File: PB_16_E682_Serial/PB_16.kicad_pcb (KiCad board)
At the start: 2 copper layers, 58 x 33 mm, 16 parts, among them J1 DMX1 RJ45, J2 DMX2 RJ45, J3 Serial In, SW1 DMX_Renard_Select, SW2 DMX_LOR_Select, U1 UA9638CP

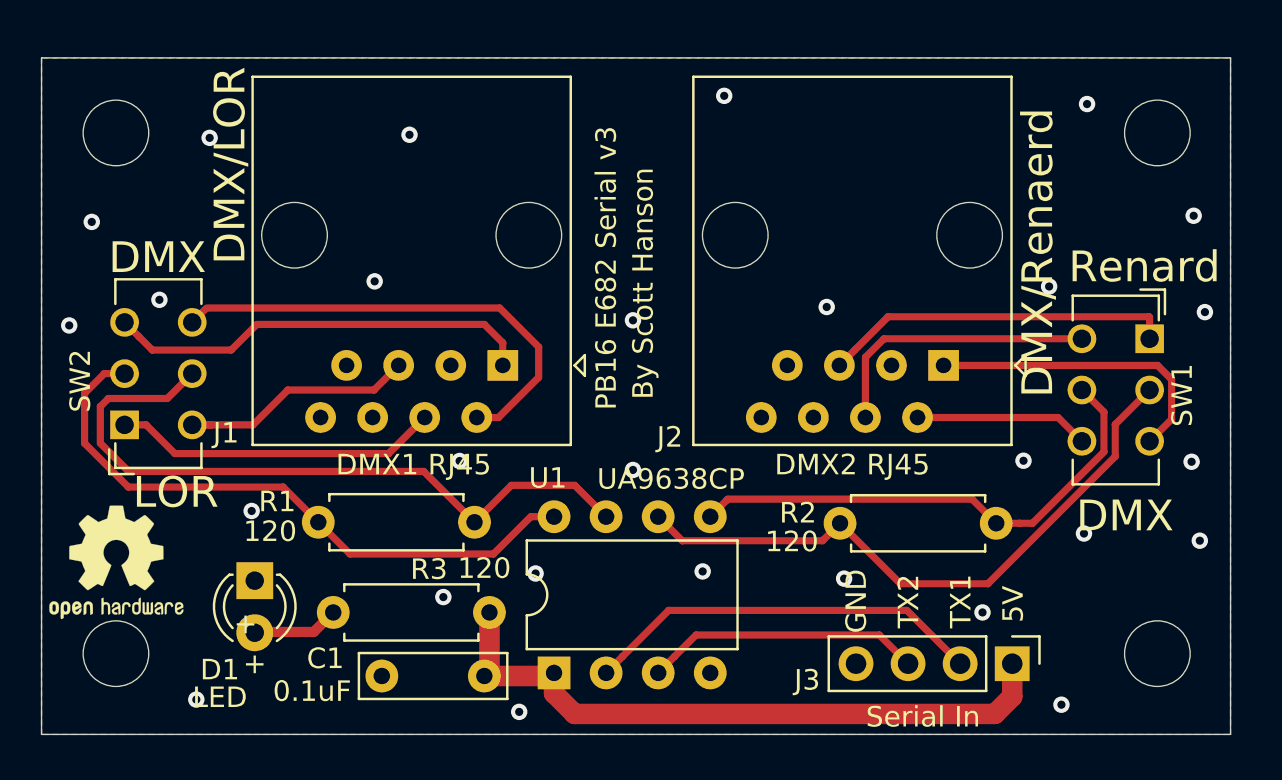
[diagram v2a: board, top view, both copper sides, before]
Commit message: increased mounting hole size
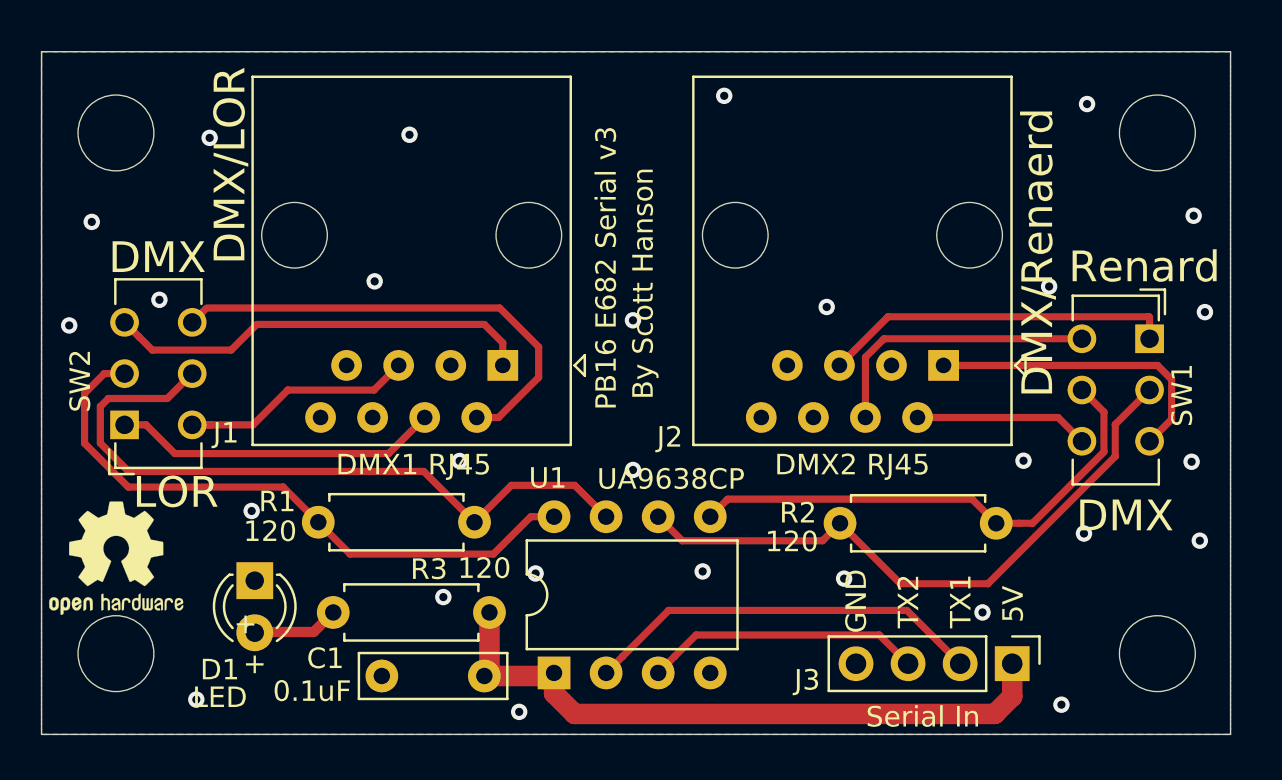
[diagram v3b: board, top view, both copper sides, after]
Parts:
- REF** (x4): value MountingHole_3.2mm_M3 -> MountingHole_3.7mm; footprint MountingHole:MountingHole_3.2mm_M3 -> MountingHole:MountingHole_3.7mm
- moved REF** 0.20 mm to (87.6, 94.4)
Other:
- board size 58 x 33 mm -> 58 x 33.3 mm
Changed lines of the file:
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@@
     (uvia_drill 0.1)
+  )
+  (module MountingHole:MountingHole_3.7mm (layer F.Cu)
+    (at 138.43 99.06)
+    (descr "Mounting Hole 3.7mm, no annular")
+    (tags "mounting hole 3.7mm no annular")
+    (attr virtual)
+    (fp_text reference REF** (at 0.57 5.94) (layer F.Fab)
+      (effects (font (size 1 1) (thickness 0.15)))
+    )
+    (fp_text value MountingHole_3.7mm (at 5.57 -4.06 90) (layer F.Fab)
+      (effects (font (size 1 1) (thickness 0.15)))
+    )
+    (fp_circle (center 0 0) (end 3.95 0) (layer F.CrtYd) (width 0.05))
+    (fp_circle (center 0 0) (end 3.7 0) (layer Cmts.User) (width 0.15))
+    (fp_text user %R (at 0.3 0) (layer F.Fab)
+      (effects (font (size 1 1) (thickness 0.15)))
+    )
+    (pad 1 np_thru_hole circle (at 0 0) (size 3.7 3.7) (drill 3.7) (layers *.Cu *.Mask))
+  )
+  (module MountingHole:MountingHole_3.7mm (layer F.Cu)
+    (at 138.43 73.66)
+    (descr "Mounting Hole 3.7mm, no annular")
+    (tags "mounting hole 3.7mm no annular")
+    (attr virtual)
+    (fp_text reference REF** (at 0 -4.2) (layer F.Fab)
+      (effects (font (size 1 1) (thickness 0.15)))
+    )
+    (fp_text value MountingHole_3.7mm (at -2.43 -6.66) (layer F.Fab)
+      (effects (font (size 1 1) (thickness 0.15)))
+    )
+    (fp_circle (center 0 0) (end 3.95 0) (layer F.CrtYd) (width 0.05))
+    (fp_circle (center 0 0) (end 3.7 0) (layer Cmts.User) (width 0.15))
+    (fp_text user %R (at 0.3 0) (layer F.Fab)
+      (effects (font (size 1 1) (thickness 0.15)))
+    )
+    (pad 1 np_thru_hole circle (at 0 0) (size 3.7 3.7) (drill 3.7) (layers *.Cu *.Mask))
+  )
+  (module MountingHole:MountingHole_3.7mm (layer F.Cu)
+    (at 87.63 73.66)
+    (descr "Mounting Hole 3.7mm, no annular")
+    (tags "mounting hole 3.7mm no annular")
+    (attr virtual)
+    (fp_text reference REF** (at -1.63 -5.66) (layer F.Fab)
+      (effects (font (size 1 1) (thickness 0.15)))
+    )
+    (fp_text value MountingHole_3.7mm (at -0.63 -4.66) (layer F.Fab)
+      (effects (font (size 1 1) (thickness 0.15)))
+    )
+    (fp_circle (center 0 0) (end 3.95 0) (layer F.CrtYd) (width 0.05))
+    (fp_circle (center 0 0) (end 3.7 0) (layer Cmts.User) (width 0.15))
+    (fp_text user %R (at 0.3 0) (layer F.Fab)
+      (effects (font (size 1 1) (thickness 0.15)))
+    )
+    (pad 1 np_thru_hole circle (at 0 0) (size 3.7 3.7) (drill 3.7) (layers *.Cu *.Mask))
+  )
+  (module MountingHole:MountingHole_3.7mm (layer F.Cu)
+    (at 87.63 99.06)
+    (descr "Mounting Hole 3.7mm, no annular")
+    (tags "mounting hole 3.7mm no annular")
+    (attr virtual)
+    (fp_text reference REF** (at -6.63 2.94) (layer F.Fab)
+      (effects (font (size 1 1) (thickness 0.15)))
+    )
+    (fp_text value MountingHole_3.7mm (at 3.37 6.94) (layer F.Fab)
+      (effects (font (size 1 1) (thickness 0.15)))
+    )
+    (fp_circle (center 0 0) (end 3.95 0) (layer F.CrtYd) (width 0.05))
+    (fp_circle (center 0 0) (end 3.7 0) (layer Cmts.User) (width 0.15))
+    (fp_text user %R (at 0.3 0) (layer F.Fab)
+      (effects (font (size 1 1) (thickness 0.15)))
+    )
+    (pad 1 np_thru_hole circle (at 0 0) (size 3.7 3.7) (drill 3.7) (layers *.Cu *.Mask))
   )
   (module Connector_RJ:RJ45_Amphenol_54602-x08_Horizontal (layer F.Cu)
@@
   )
   (module Symbol:OSHW-Logo2_7.3x6mm_SilkScreen (layer F.Cu)
-    (at 87.65 94.6)
+    (at 87.6427 94.3991)
     (descr "Open Source Hardware Symbol")
     (tags "Logo Symbol OSHW")
@@
       (xy -2.549664 1.91989) (xy -2.469928 1.911165) (xy -2.400256 1.919918)) (layer F.SilkS) (width 0.01))
   )
-  (module MountingHole:MountingHole_3.2mm_M3 (layer F.Cu)
-    (at 138.43 99.06)
-    (descr "Mounting Hole 3.2mm, no annular, M3")
-    (tags "mounting hole 3.2mm no annular m3")
-    (attr virtual)
-    (fp_text reference REF** (at 0.57 5.94) (layer F.Fab)
-      (effects (font (size 1 1) (thickness 0.15)))
-    )
-    (fp_text value MountingHole_3.2mm_M3 (at 5.57 -4.06 90) (layer F.Fab)
-      (effects (font (size 1 1) (thickness 0.15)))
-    )
-    (fp_circle (center 0 0) (end 3.45 0) (layer F.CrtYd) (width 0.05))
-    (fp_circle (center 0 0) (end 3.2 0) (layer Cmts.User) (width 0.15))
-    (fp_text user %R (at 0.3 0) (layer F.Fab)
-      (effects (font (size 1 1) (thickness 0.15)))
-    )
-    (pad 1 np_thru_hole circle (at 0 0) (size 3.2 3.2) (drill 3.2) (layers *.Cu *.Mask))
-  )
-  (module MountingHole:MountingHole_3.2mm_M3 (layer F.Cu)
-    (at 138.43 73.66)
-    (descr "Mounting Hole 3.2mm, no annular, M3")
-    (tags "mounting hole 3.2mm no annular m3")
-    (attr virtual)
-    (fp_text reference REF** (at 0 -4.2) (layer F.Fab)
-      (effects (font (size 1 1) (thickness 0.15)))
-    )
-    (fp_text value MountingHole_3.2mm_M3 (at -2.43 -6.66) (layer F.Fab)
-      (effects (font (size 1 1) (thickness 0.15)))
-    )
-    (fp_text user %R (at 0.3 0) (layer F.Fab)
-      (effects (font (size 1 1) (thickness 0.15)))
-    )
-    (fp_circle (center 0 0) (end 3.2 0) (layer Cmts.User) (width 0.15))
-    (fp_circle (center 0 0) (end 3.45 0) (layer F.CrtYd) (width 0.05))
-    (pad 1 np_thru_hole circle (at 0 0) (size 3.2 3.2) (drill 3.2) (layers *.Cu *.Mask))
-  )
-  (module MountingHole:MountingHole_3.2mm_M3 (layer F.Cu)
-    (at 87.63 73.66)
-    (descr "Mounting Hole 3.2mm, no annular, M3")
-    (tags "mounting hole 3.2mm no annular m3")
-    (attr virtual)
-    (fp_text reference REF** (at -1.63 -5.66) (layer F.Fab)
-      (effects (font (size 1 1) (thickness 0.15)))
-    )
-    (fp_text value MountingHole_3.2mm_M3 (at -0.63 -4.66) (layer F.Fab)
-      (effects (font (size 1 1) (thickness 0.15)))
-    )
-    (fp_text user %R (at 0.3 0) (layer F.Fab)
-      (effects (font (size 1 1) (thickness 0.15)))
-    )
-    (fp_circle (center 0 0) (end 3.2 0) (layer Cmts.User) (width 0.15))
-    (fp_circle (center 0 0) (end 3.45 0) (layer F.CrtYd) (width 0.05))
-    (pad 1 np_thru_hole circle (at 0 0) (size 3.2 3.2) (drill 3.2) (layers *.Cu *.Mask))
-  )
-  (module MountingHole:MountingHole_3.2mm_M3 (layer F.Cu)
-    (at 87.63 99.06)
-    (descr "Mounting Hole 3.2mm, no annular, M3")
-    (tags "mounting hole 3.2mm no annular m3")
-    (attr virtual)
-    (fp_text reference REF** (at -6.63 2.94) (layer F.Fab)
-      (effects (font (size 1 1) (thickness 0.15)))
-    )
-    (fp_text value MountingHole_3.2mm_M3 (at 3.37 6.94) (layer F.Fab)
-      (effects (font (size 1 1) (thickness 0.15)))
-    )
-    (fp_circle (center 0 0) (end 3.45 0) (layer F.CrtYd) (width 0.05))
-    (fp_circle (center 0 0) (end 3.2 0) (layer Cmts.User) (width 0.15))
-    (fp_text user %R (at 0.3 0) (layer F.Fab)
-      (effects (font (size 1 1) (thickness 0.15)))
-    )
-    (pad 1 np_thru_hole circle (at 0 0) (size 3.2 3.2) (drill 3.2) (layers *.Cu *.Mask))
-  )
   (module Package_DIP:DIP-8_W7.62mm (layer F.Cu)
     (at 109 100 90)
@@
   (gr_line (start 138.43 99.06) (end 138.43 73.66) (layer F.Fab) (width 0.12))
   (gr_line (start 87.63 99.06) (end 138.43 99.06) (layer F.Fab) (width 0.12))
-  (gr_line (start 84 103) (end 84 70) (layer Edge.Cuts) (width 0.05))
+  (gr_line (start 84 103) (end 83.9987 69.6976) (layer Edge.Cuts) (width 0.05))
   (gr_line (start 142 103) (end 84 103) (layer Edge.Cuts) (width 0.05))
-  (gr_line (start 142 70) (end 142 103) (layer Edge.Cuts) (width 0.05))
-  (gr_line (start 84 70) (end 142 70) (layer Edge.Cuts) (width 0.05))
+  (gr_line (start 141.9987 69.6976) (end 142 103) (layer Edge.Cuts) (width 0.05))
+  (gr_line (start 83.9987 69.6976) (end 141.9987 69.6976) (layer Edge.Cuts) (width 0.05))
   (via (at 133.75 101.55) (size 0.8) (drill 0.4) (layers F.Cu B.Cu) (net 1))
   (via (at 140.5 93.55) (size 0.8) (drill 0.4) (layers F.Cu B.Cu) (net 1))
@@
     (polygon
       (pts
-        (xy 84 70) (xy 142 70) (xy 142 103) (xy 84 103)
+        (xy 84 69.6976) (xy 142 69.6976) (xy 142 103) (xy 84 103)
       )
     )
@@
     (polygon
       (pts
-        (xy 142 103) (xy 142 70) (xy 84 70) (xy 84 103)
+        (xy 142 103) (xy 141.9987 69.6976) (xy 84.0105 69.6976) (xy 84 103)
       )
     )

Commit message: update to kicad v9
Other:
- net class 3.3v removed
- net class 5v removed
- net class 9v removed
- net class Default removed
- net class Gnd removed
- net class Power removed
- net class Vin removed
- net class power2 removed
